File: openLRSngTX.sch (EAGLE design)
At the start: 32 parts, among them IC1 RFM23BPSMD, J1 AVR_SPI_PRG_6PTH, Q1 MMBT2222, U1 ATMEGA328P, X1 BU-SMA-V, Y1 16MHz

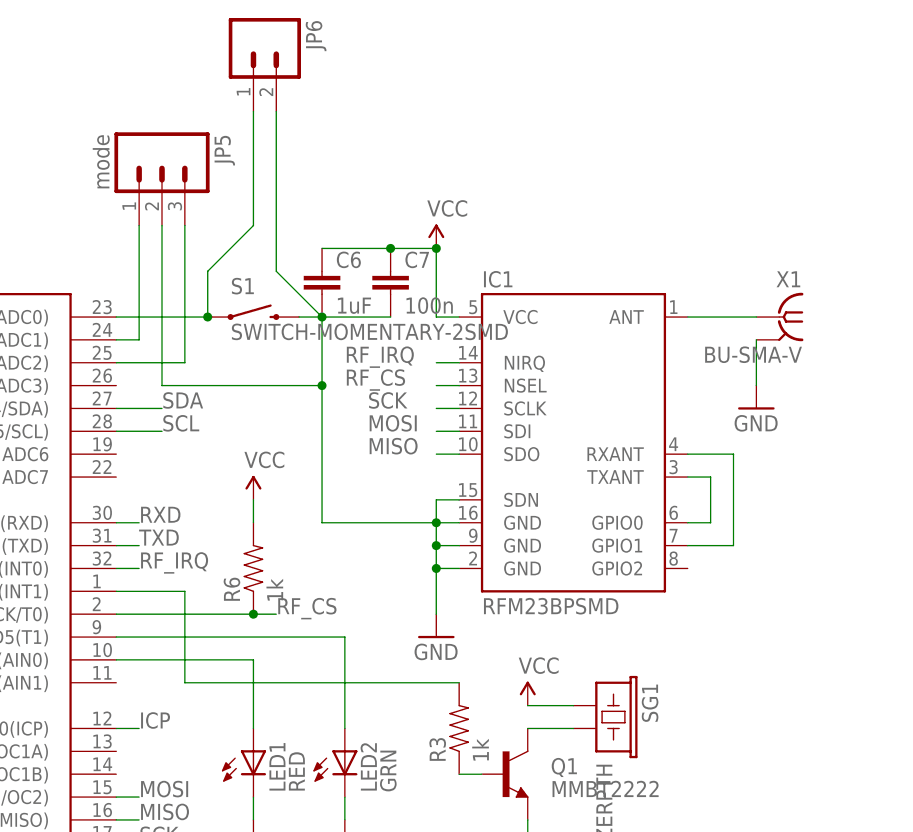
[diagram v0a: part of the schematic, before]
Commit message: Add mountting holes.
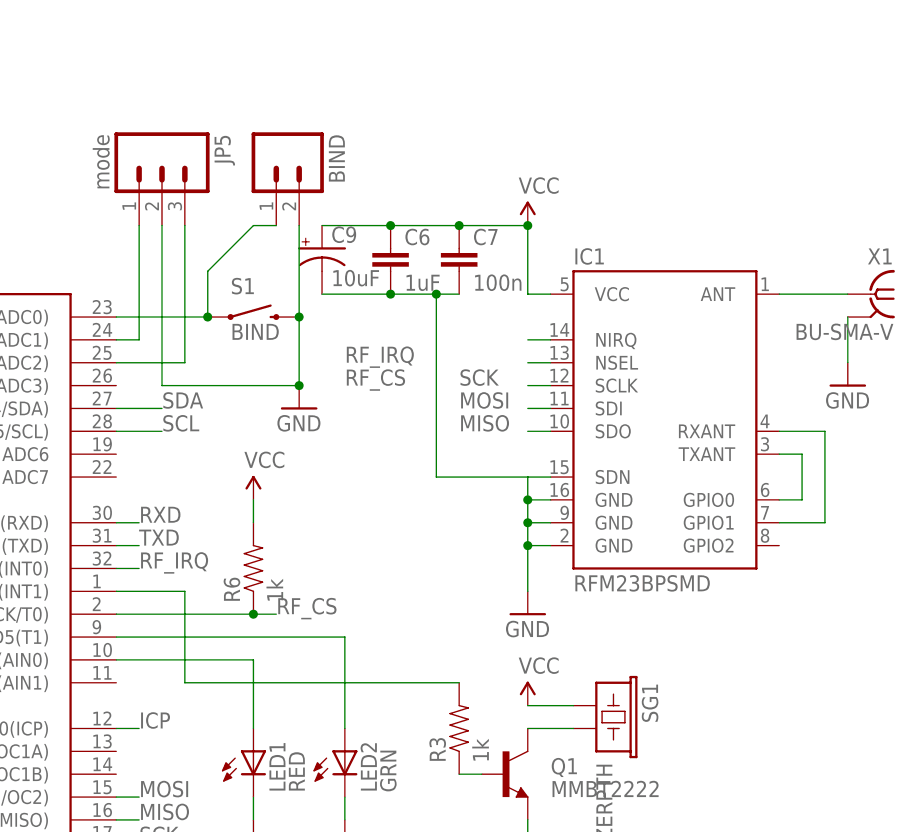
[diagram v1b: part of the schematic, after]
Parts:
- removed JP6: (no value), SparkFun-Connectors:M02PTH
- added BIND: (no value), SparkFun-Connectors:M02PTH
- added C9: 10uF, SparkFun-Capacitors:10UF-TANT
- S1: value SWITCH-MOMENTARY-2SMD -> BIND
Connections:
- net GND: now also BIND.2, C9.-; no longer JP6.2
- net N$15: now also BIND.1; no longer JP6.1
- net VCC: now also C9.+
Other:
- moved on the sheet: C6, C7, IC1, X1

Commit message: rev2 modifications
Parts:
- removed C3: 1uF, SparkFun-Capacitors:CAP0805
- removed C9: 10uF, SparkFun-Capacitors:10UF-TANT
- removed JP4: REG, SparkFun-Connectors:M03PTH
- added C10: (no value), rcl:CPOL-EUD/7343-31W
- added D1: (no value), diode:DIODE-DO214AC
- added IC2: LT1173CS8, ltc_swr:LT1173CS8
- added L1: DR74, inductors:DR74
- added R10: 12k, SparkFun-Resistors:RESISTOR0805-RES
- added R11: x, SparkFun-Resistors:RESISTOR0805-RES
- added R9: 270k, SparkFun-Resistors:RESISTOR0805-RES
- S1: device SparkFun-Electromechanical:SWITCH-MOMENTARY-2SMD -> SparkFun-Electromechanical:SWITCH-MOMENTARY-2
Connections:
- new net N$21: D1.C, IC2.SW2, L1.1
- new net N$25: IC2.FB, R10.2, R11.2, R9.1
- new net VCN: R11.1, U1.PD7(AIN1)
- net GND: now also C10.-, D1.A, IC2.GND, JP1.4, LED1.C, LED2.C, R10.1; no longer C3.2, C9.-, JP1.2, JP4.2, R4.1, R5.1
- net N$10: now also LED1.A, R4.1; no longer LED2.C, R5.2
- net N$17: now also JP1.2; no longer JP1.4
- net N$7: now also R4.2; no longer LED1.A
- net N$8: now also R5.2; no longer LED2.A
- net N$9: now also LED2.A, R5.1; no longer LED1.C, R4.2
- net RAW: now also IC2.I_LIM, IC2.SW1, IC2.V_IN; no longer JP4.1
- net RXD: now also R7.2; no longer R8.2
- net TXD: now also R8.2; no longer R7.2
- net VCC: now also C10.+, L1.2, R9.2; no longer C3.1, C9.+, JP4.3
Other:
- moved on the sheet: C2, LED1, LED2, R4, R5, R7

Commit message: Cleanups, this should be it for rev2
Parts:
- added C3: 12pF, SparkFun-Capacitors:CAP0805
- added C9: 1uF, SparkFun-Capacitors:CAP0805
- BIND: value (none) -> BIND
- C1: value 100n -> 1uF
- C10: value (none) -> 100n; device rcl:CPOL-EUD/7343-31W -> SparkFun-Capacitors:CAP0805
- C5: value 12pF -> 100n
- C6: value 1uF -> 100n
- C8: value 100n -> 100uF; device SparkFun-Capacitors:CAP0805 -> rcl:CPOL-EUD/7343-31W
- D1: value (none) -> 1N5819
- IC1: value RFM23BPSMD -> LT1073CS8; device RFM23:RFM23BPSMD -> ltc_swr:LT1173CS8
- IC2: value LT1173CS8 -> RFM23BPSMD; device ltc_swr:LT1173CS8 -> RFM23:RFM23BPSMD
- R1: value 10k -> 1k
- R10: value 12k -> 220R
- R11: value x -> 1k
- R4: value 220R -> 10k
- R5: value 220R -> x
- R6: value 1k -> 270k
- R7: value 1k -> 12k
- R9: value 270k -> 220R
- renumbered JP5 to JP4
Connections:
- net /RESET: now also C5.2, R4.1; no longer C1.2, R1.1
- net DTR: now also C5.1; no longer C1.1
- net GND: now also C1.2, C10.2, C3.2, C6.1, C8.-, C9.2, IC1.GND, IC2.GND@1, IC2.GND@2, IC2.GND@3, IC2.SDN, R7.1; no longer C10.-, C5.2, C6.2, C8.1, IC1.GND@1, IC1.GND@2, IC1.GND@3, IC1.SDN, IC2.GND, R10.1
- net MISO: now also IC2.SDO; no longer IC1.SDO
- net MOSI: now also IC2.SDI; no longer IC1.SDI
- net N$1: now also IC2.GPIO0, IC2.TXANT; no longer IC1.GPIO0, IC1.TXANT
- net N$10: now also R9.1; no longer R4.1
- net N$11: now also C3.1; no longer C4.1
- net N$12: now also C4.1; no longer C5.1
- net N$13: now also IC2.ANT; no longer IC1.ANT
- net N$14: now also C6.2; no longer C8.2
- net N$17: now also R3.1; no longer R7.1
- net N$2: now also IC2.GPIO1, IC2.RXANT; no longer IC1.GPIO1, IC1.RXANT
- net N$20: now also R1.1; no longer R8.1
- net N$21: now also IC1.SW2; no longer IC2.SW2
- net N$25: now also IC1.FB, R5.2, R6.1, R7.2; no longer IC2.FB, R10.2, R11.2, R9.1
- net N$4: now also R11.2; no longer R3.2
- net N$5: now also R11.1; no longer R3.1
- net N$7: now also R9.2; no longer R4.2
- net N$8: now also R10.2; no longer R5.2
- net N$9: now also R10.1; no longer R5.1
- net RAW: now also C1.1, IC1.I_LIM, IC1.SW1, IC1.V_IN; no longer IC2.I_LIM, IC2.SW1, IC2.V_IN
- net RF_CS: now also IC2.NSEL, R8.1; no longer IC1.NSEL, R6.1
- net RF_IRQ: now also IC2.NIRQ; no longer IC1.NIRQ
- net RXD: now also R3.2; no longer R7.2
- net SCK: now also IC2.SCLK; no longer IC1.SCLK
- net TXD: now also R1.2; no longer R8.2
- net VCC: now also C10.1, C8.+, C9.1, IC2.VCC, R4.2, R8.2; no longer C10.+, C6.1, IC1.VCC, R1.2, R9.2
- net VCN: now also R5.1; no longer R11.1
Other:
- moved on the sheet: C1, C2, C4, C5, C6, C7, R1, R10, R11, R3, R4, R5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

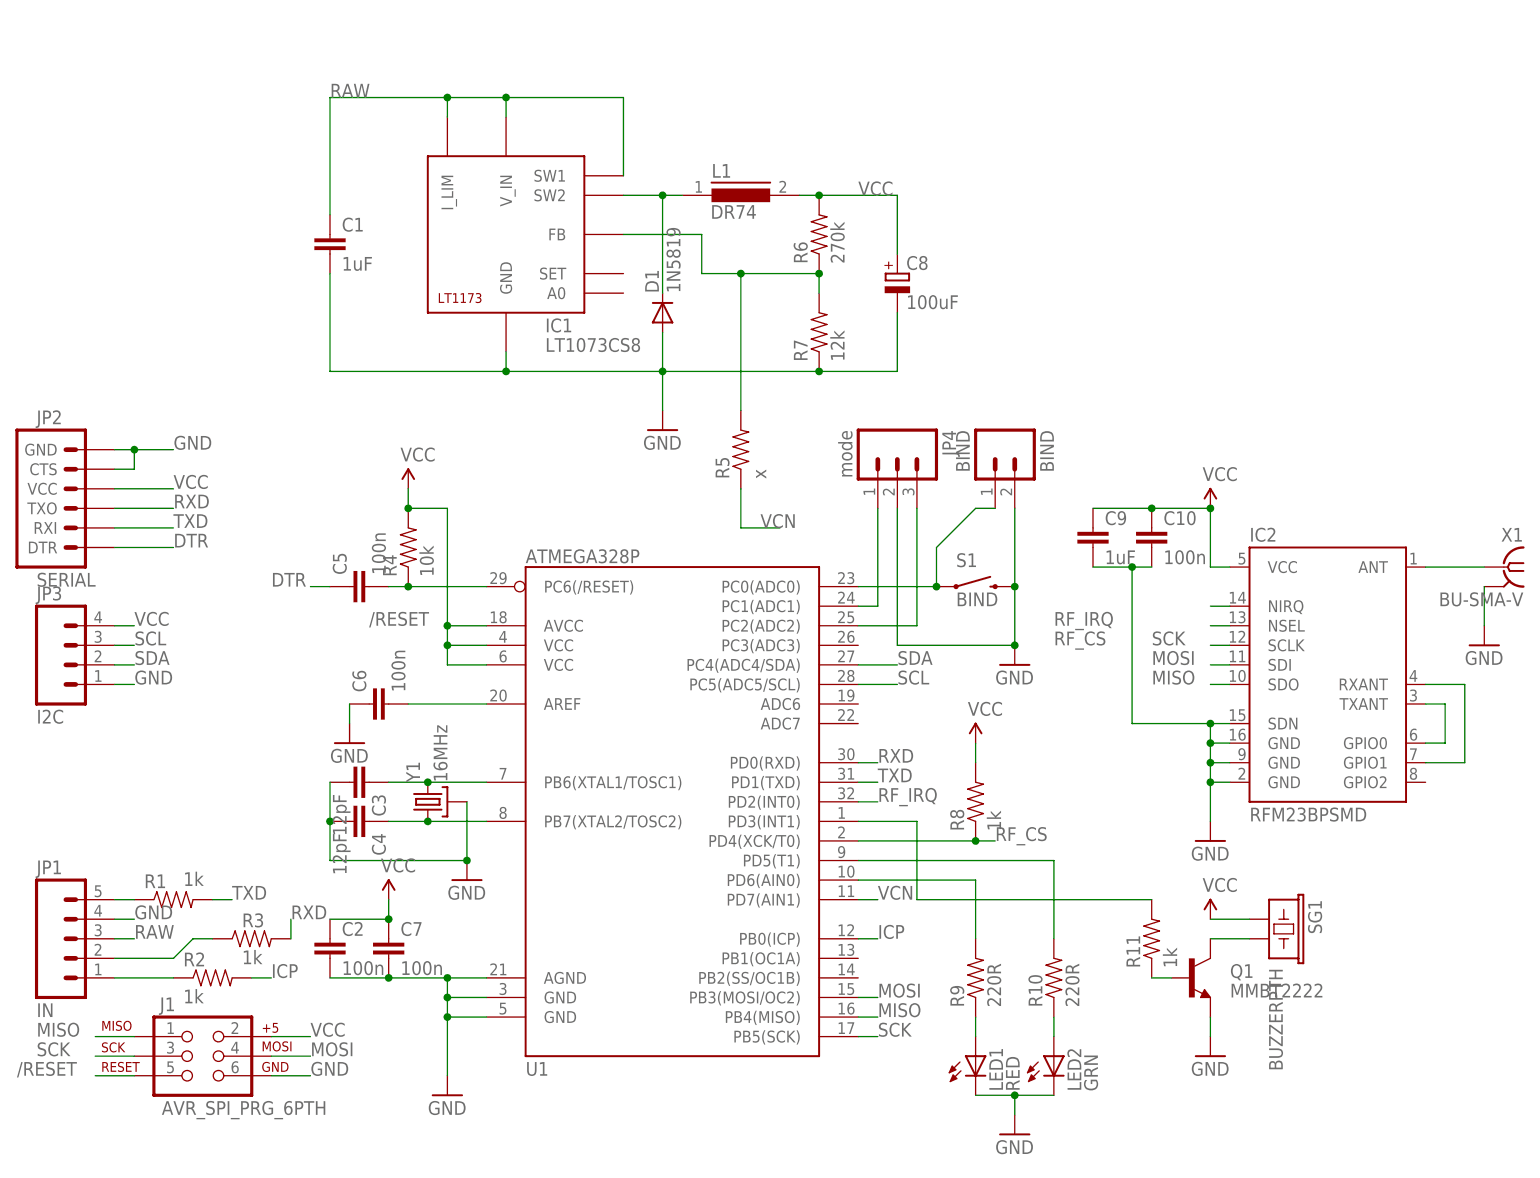
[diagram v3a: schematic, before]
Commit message: Revised the DCDC section and added possibility for smaller buzzer.
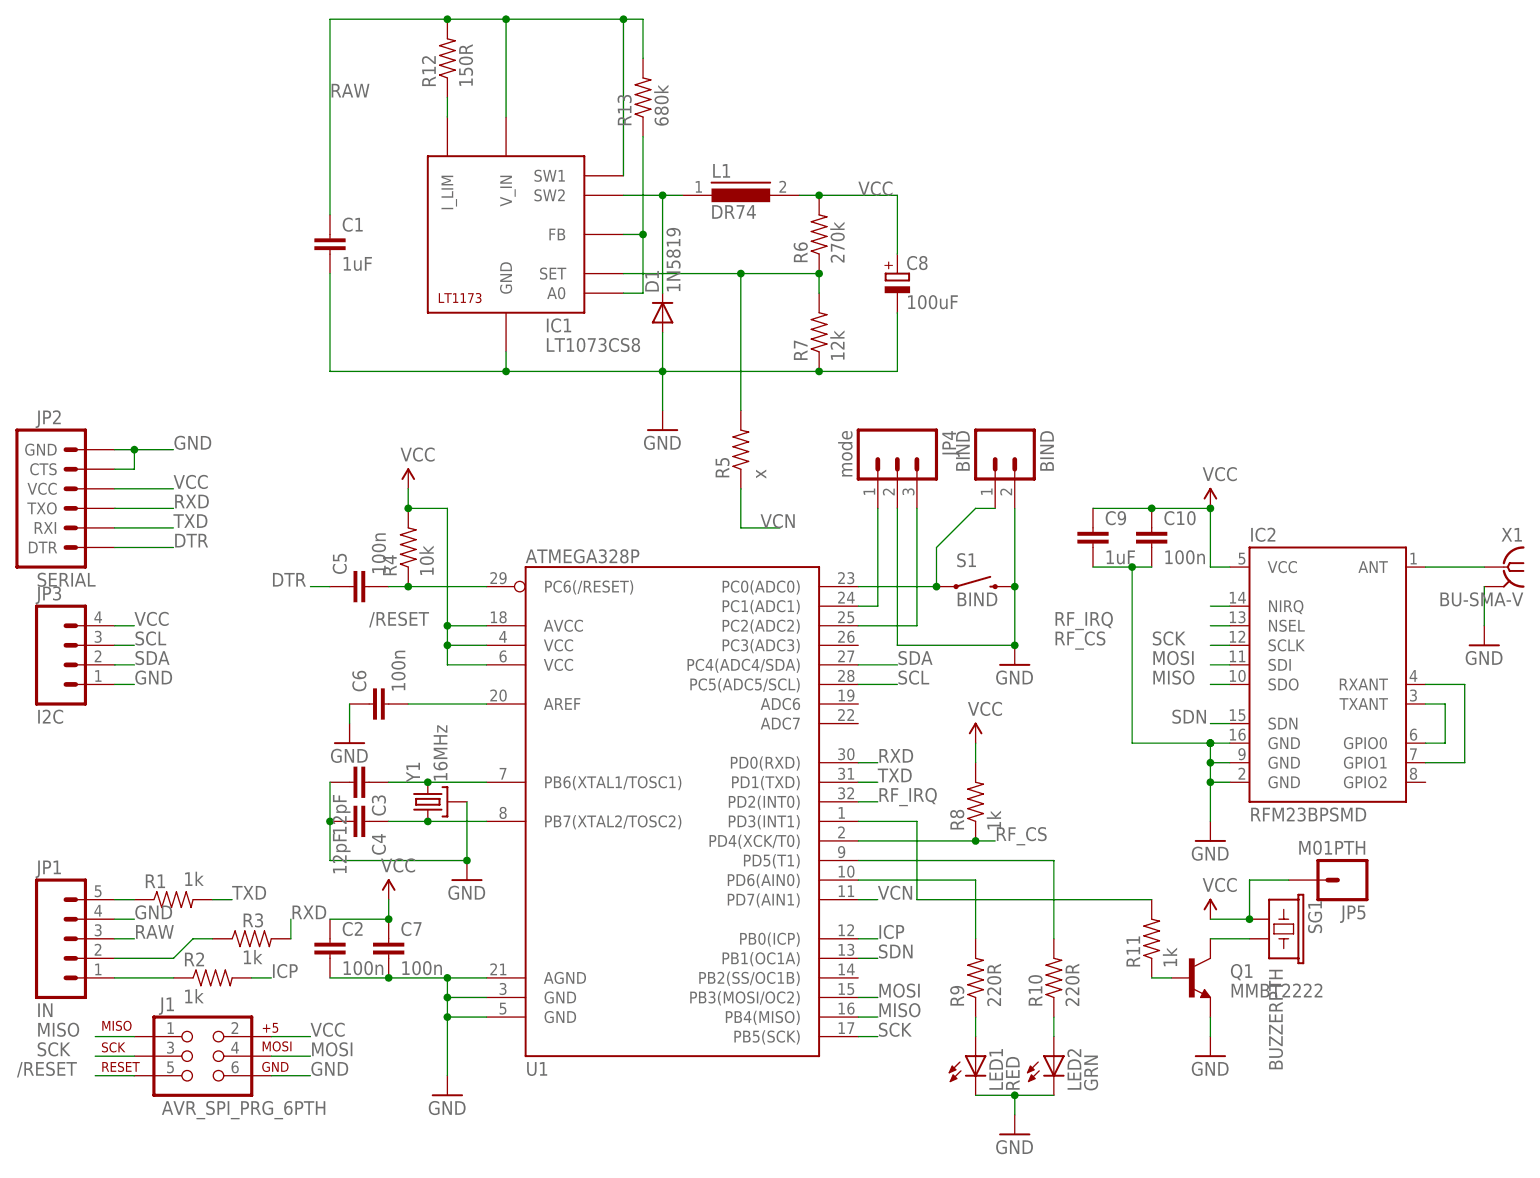
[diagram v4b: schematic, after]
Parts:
- added JP5: M01PTH, SparkFun-Connectors:M01PTH
- added R12: 150R, SparkFun-Resistors:RESISTOR0805-RES
- added R13: 680k, SparkFun-Resistors:RESISTOR0805-RES
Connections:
- new net N$16: IC1.I_LIM, R12.1
- new net N$22: IC1.A0, IC1.FB, R13.1
- new net SDN: IC2.SDN, U1.PB1(OC1A)
- net GND: no longer IC2.SDN
- net N$25: now also IC1.SET; no longer IC1.FB
- net RAW: now also R12.2, R13.2; no longer IC1.I_LIM
- net VCC: now also JP5.1
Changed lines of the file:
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@@
 <part name="C2" library="SparkFun-Capacitors" deviceset="CAP" device="0805" value="100n"/>
 <part name="C1" library="SparkFun-Capacitors" deviceset="CAP" device="0805" value="1uF"/>
+<part name="R12" library="SparkFun-Resistors" deviceset="RESISTOR" device="0805-RES" value="150R"/>
+<part name="R13" library="SparkFun-Resistors" deviceset="RESISTOR" device="0805-RES" value="680k"/>
+<part name="JP5" library="SparkFun-Connectors" deviceset="M01" device="PTH"/>
 </parts>
 <sheets>
@@
 <instance part="C2" gate="G$1" x="22.86" y="43.18"/>
 <instance part="C1" gate="G$1" x="22.86" y="134.62"/>
+<instance part="R12" gate="G$1" x="38.1" y="160.02" rot="R90"/>
+<instance part="R13" gate="G$1" x="63.5" y="154.94" rot="R90"/>
+<instance part="JP5" gate="G$1" x="154.94" y="53.34" rot="R180"/>
 </instances>
 <busses>
@@
 <pinref part="IC2" gate="G$1" pin="GND@2"/>
 <wire x1="139.7" y1="68.58" x2="137.16" y2="68.58" width="0.1524" layer="91"/>
-<pinref part="IC2" gate="G$1" pin="SDN"/>
-<wire x1="137.16" y1="73.66" x2="139.7" y2="73.66" width="0.1524" layer="91"/>
 <pinref part="IC2" gate="G$1" pin="GND@3"/>
 <wire x1="139.7" y1="71.12" x2="137.16" y2="71.12" width="0.1524" layer="91"/>
-<wire x1="137.16" y1="71.12" x2="137.16" y2="73.66" width="0.1524" layer="91"/>
 <junction x="137.16" y="71.12"/>
 <wire x1="137.16" y1="71.12" x2="137.16" y2="68.58" width="0.1524" layer="91"/>
@@
 <wire x1="121.92" y1="93.98" x2="127" y2="93.98" width="0.1524" layer="91"/>
 <wire x1="127" y1="93.98" x2="129.54" y2="93.98" width="0.1524" layer="91"/>
-<wire x1="137.16" y1="73.66" x2="127" y2="73.66" width="0.1524" layer="91"/>
-<wire x1="127" y1="73.66" x2="127" y2="93.98" width="0.1524" layer="91"/>
+<wire x1="137.16" y1="71.12" x2="127" y2="71.12" width="0.1524" layer="91"/>
+<wire x1="127" y1="71.12" x2="127" y2="93.98" width="0.1524" layer="91"/>
 <junction x="127" y="93.98"/>
-<junction x="137.16" y="73.66"/>
+<junction x="137.16" y="71.12"/>
 </segment>
 <segment>
@@
 <pinref part="SG1" gate="G$1" pin="1"/>
 <wire x1="137.16" y1="48.26" x2="142.24" y2="48.26" width="0.1524" layer="91"/>
+<pinref part="JP5" gate="G$1" pin="1"/>
+<wire x1="147.32" y1="53.34" x2="142.24" y2="53.34" width="0.1524" layer="91"/>
+<wire x1="142.24" y1="53.34" x2="142.24" y2="48.26" width="0.1524" layer="91"/>
+<junction x="142.24" y="48.26"/>
 </segment>
 <segment>
@@
 <segment>
 <pinref part="IC1" gate="G$1" pin="SW1"/>
-<wire x1="60.96" y1="144.78" x2="60.96" y2="154.94" width="0.1524" layer="91"/>
-<wire x1="60.96" y1="154.94" x2="45.72" y2="154.94" width="0.1524" layer="91"/>
+<wire x1="60.96" y1="144.78" x2="60.96" y2="165.1" width="0.1524" layer="91"/>
+<wire x1="60.96" y1="165.1" x2="45.72" y2="165.1" width="0.1524" layer="91"/>
 <pinref part="IC1" gate="G$1" pin="V_IN"/>
-<wire x1="45.72" y1="154.94" x2="45.72" y2="152.4" width="0.1524" layer="91"/>
-<pinref part="IC1" gate="G$1" pin="I_LIM"/>
-<wire x1="45.72" y1="154.94" x2="38.1" y2="154.94" width="0.1524" layer="91"/>
-<wire x1="38.1" y1="154.94" x2="38.1" y2="152.4" width="0.1524" layer="91"/>
-<wire x1="38.1" y1="154.94" x2="22.86" y2="154.94" width="0.1524" layer="91"/>
+<wire x1="45.72" y1="165.1" x2="45.72" y2="152.4" width="0.1524" layer="91"/>
+<wire x1="45.72" y1="165.1" x2="38.1" y2="165.1" width="0.1524" layer="91"/>
 <label x="22.86" y="154.94" size="1.778" layer="95"/>
-<junction x="38.1" y="154.94"/>
-<junction x="45.72" y="154.94"/>
+<junction x="45.72" y="165.1"/>
 <pinref part="C1" gate="G$1" pin="1"/>
-<wire x1="22.86" y1="139.7" x2="22.86" y2="154.94" width="0.1524" layer="91"/>
+<wire x1="38.1" y1="165.1" x2="22.86" y2="165.1" width="0.1524" layer="91"/>
+<wire x1="22.86" y1="139.7" x2="22.86" y2="165.1" width="0.1524" layer="91"/>
+<pinref part="R12" gate="G$1" pin="2"/>
+<junction x="38.1" y="165.1"/>
+<pinref part="R13" gate="G$1" pin="2"/>
+<wire x1="63.5" y1="160.02" x2="63.5" y2="165.1" width="0.1524" layer="91"/>
+<wire x1="63.5" y1="165.1" x2="60.96" y2="165.1" width="0.1524" layer="91"/>
+<junction x="60.96" y="165.1"/>
 </segment>
 </net>
@@
 <wire x1="86.36" y1="129.54" x2="86.36" y2="132.08" width="0.1524" layer="91"/>
 <wire x1="86.36" y1="132.08" x2="76.2" y2="132.08" width="0.1524" layer="91"/>
-<wire x1="76.2" y1="132.08" x2="71.12" y2="132.08" width="0.1524" layer="91"/>
-<wire x1="71.12" y1="132.08" x2="71.12" y2="137.16" width="0.1524" layer="91"/>
-<pinref part="IC1" gate="G$1" pin="FB"/>
-<wire x1="71.12" y1="137.16" x2="60.96" y2="137.16" width="0.1524" layer="91"/>
 <junction x="86.36" y="132.08"/>
 <pinref part="R5" gate="G$1" pin="2"/>
 <wire x1="76.2" y1="114.3" x2="76.2" y2="132.08" width="0.1524" layer="91"/>
+<pinref part="IC1" gate="G$1" pin="SET"/>
+<wire x1="60.96" y1="132.08" x2="76.2" y2="132.08" width="0.1524" layer="91"/>
 <junction x="76.2" y="132.08"/>
 </segment>
@@
 </segment>
 </net>
+<net name="N$16" class="0">
+<segment>
+<pinref part="R12" gate="G$1" pin="1"/>
+<pinref part="IC1" gate="G$1" pin="I_LIM"/>
+<wire x1="38.1" y1="154.94" x2="38.1" y2="152.4" width="0.1524" layer="91"/>
+</segment>
+</net>
+<net name="N$22" class="0">
+<segment>
+<pinref part="IC1" gate="G$1" pin="A0"/>
+<wire x1="60.96" y1="129.54" x2="63.5" y2="129.54" width="0.1524" layer="91"/>
+<wire x1="63.5" y1="129.54" x2="63.5" y2="137.16" width="0.1524" layer="91"/>
+<pinref part="IC1" gate="G$1" pin="FB"/>
+<wire x1="63.5" y1="137.16" x2="60.96" y2="137.16" width="0.1524" layer="91"/>
+<pinref part="R13" gate="G$1" pin="1"/>
+<wire x1="63.5" y1="149.86" x2="63.5" y2="137.16" width="0.1524" layer="91"/>
+<junction x="63.5" y="137.16"/>
+</segment>
+</net>
+<net name="SDN" class="0">
+<segment>
+<pinref part="IC2" gate="G$1" pin="SDN"/>
+<wire x1="139.7" y1="73.66" x2="137.16" y2="73.66" width="0.1524" layer="91"/>
+<label x="132.08" y="73.66" size="1.778" layer="95"/>
+</segment>
+<segment>
+<pinref part="U1" gate="G$1" pin="PB1(OC1A)"/>
+<wire x1="91.44" y1="43.18" x2="93.98" y2="43.18" width="0.1524" layer="91"/>
+<label x="93.98" y="43.18" size="1.778" layer="95"/>
+</segment>
+</net>
